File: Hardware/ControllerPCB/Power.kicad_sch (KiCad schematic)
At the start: 46 parts, among them Q1 SQJ146ELP, U2 BTN9960LV, U3 BTN9960LV, U4 INA180A2, U6 TSR 0.5-2433

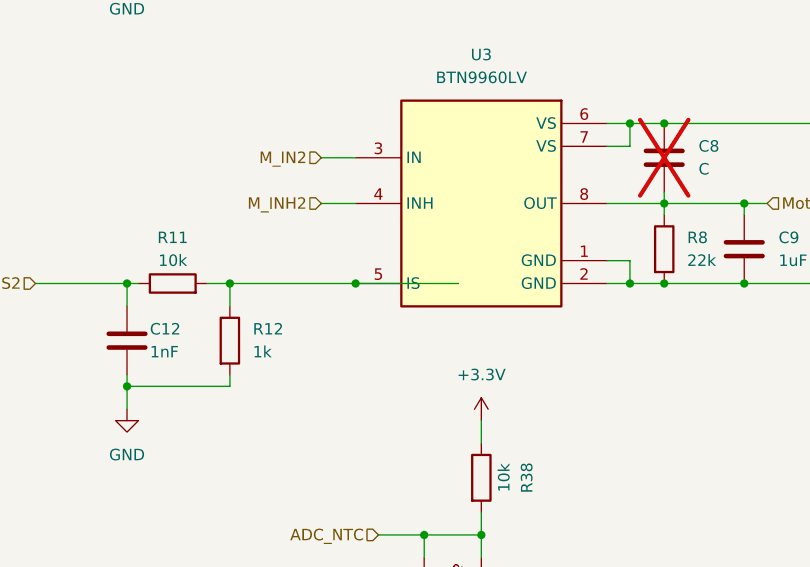
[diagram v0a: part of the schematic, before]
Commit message: fix schematics and pins for the encoder
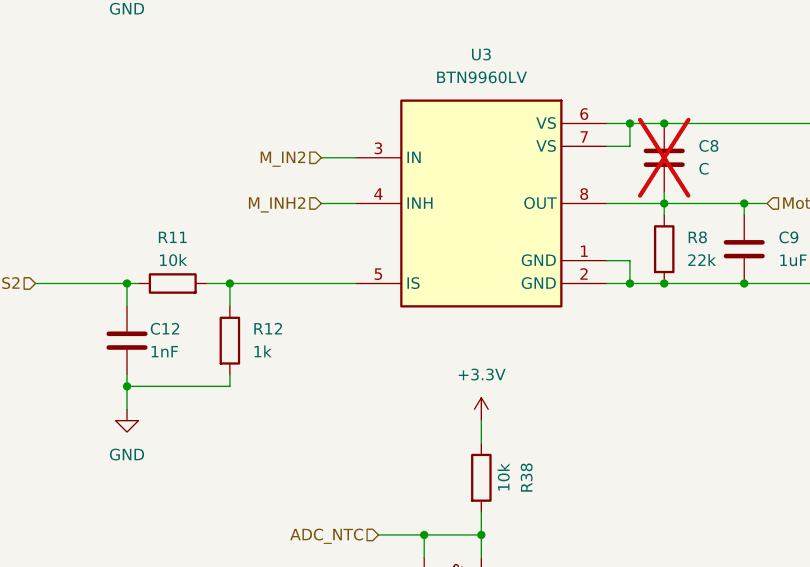
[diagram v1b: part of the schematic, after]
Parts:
- C10, C24, C25, C26, C7: footprint Capacitor_SMD:C_1206_3216Metric -> BugWiper_lib:C_1206_3216Metric
- C11, C12, C13, C14, C31, C6, C8: footprint Capacitor_SMD:C_0603_1608Metric -> BugWiper_lib:C_0603_1608Metric
- C15, C16, C17, C21, C23: footprint Capacitor_SMD:C_1210_3225Metric -> BugWiper_lib:C_1210_3225Metric
- C18, C19, C20, C28: footprint Capacitor_SMD:CP_Elec_8x10.5 -> BugWiper_lib:CP_Elec_8x10.5
- C5, C9: footprint Capacitor_SMD:C_0805_2012Metric -> BugWiper_lib:C_0805_2012Metric
- D2: footprint Diode_SMD:D_SOD-323_HandSoldering -> BugWiper_lib:D_SOD-323_HandSoldering
- D3: footprint Diode_SMD:D_SMB -> BugWiper_lib:D_SMB
- R10, R11, R12, R19, R20, R21, R38, R7, R8, R9, TH1: footprint Resistor_SMD:R_0603_1608Metric -> BugWiper_lib:R_0603_1608Metric
- R25: footprint Resistor_SMD:R_1210_3225Metric -> BugWiper_lib:R_1210_3225Metric
- U4: footprint Package_TO_SOT_SMD:SOT-23-5 -> BugWiper_lib:SOT-23-5
